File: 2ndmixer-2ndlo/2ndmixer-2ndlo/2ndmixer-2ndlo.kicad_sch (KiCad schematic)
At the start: 44 parts, among them J201 Coax Solder Point, J202 Conn_01x02, J203 Coax Solder Point, Q201 2N5179, Q202 2N5109, T201 Bifilar_Transformer, U201 MAV-11BSM+, U202 TUF-1H+, Y201 100MHz

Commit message: minor fixes to 2ndmixer-2ndlo
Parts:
- C202, C203, C204, C205, C207, C208, C209, C210, C211, C212, C213, C214, C215: footprint (none) -> Capacitor_THT:C_Disc_D5.0mm_W2.5mm_P5.00mm
- C206: footprint (none) -> 2ndmixer-2ndlo:GKG60015
- L201, L202, L203: footprint (none) -> Inductor_THT:L_Toroid_Vertical_L13.0mm_W6.5mm_P5.60mm
- Q201: footprint TO127P584H533-4N -> 2ndmixer-2ndlo:TO127P584H533-4N
- Q202: footprint TO5A -> 2ndmixer-2ndlo:TO5A
- R201, R202, R203, R204, R205, R206, R207, R208, R209, R210, R211, R212, R213, R214, R215, R216, R217: footprint (none) -> Resistor_THT:R_Axial_DIN0207_L6.3mm_D2.5mm_P7.62mm_Horizontal
- T201: footprint (none) -> Transformer_THT:Autotransformer_Toroid_1Tap_Horizontal_D10.5mm_Amidon-T37
- U201: footprint RRR137_MNC -> 2ndmixer-2ndlo:MAV-11BSM&plus_

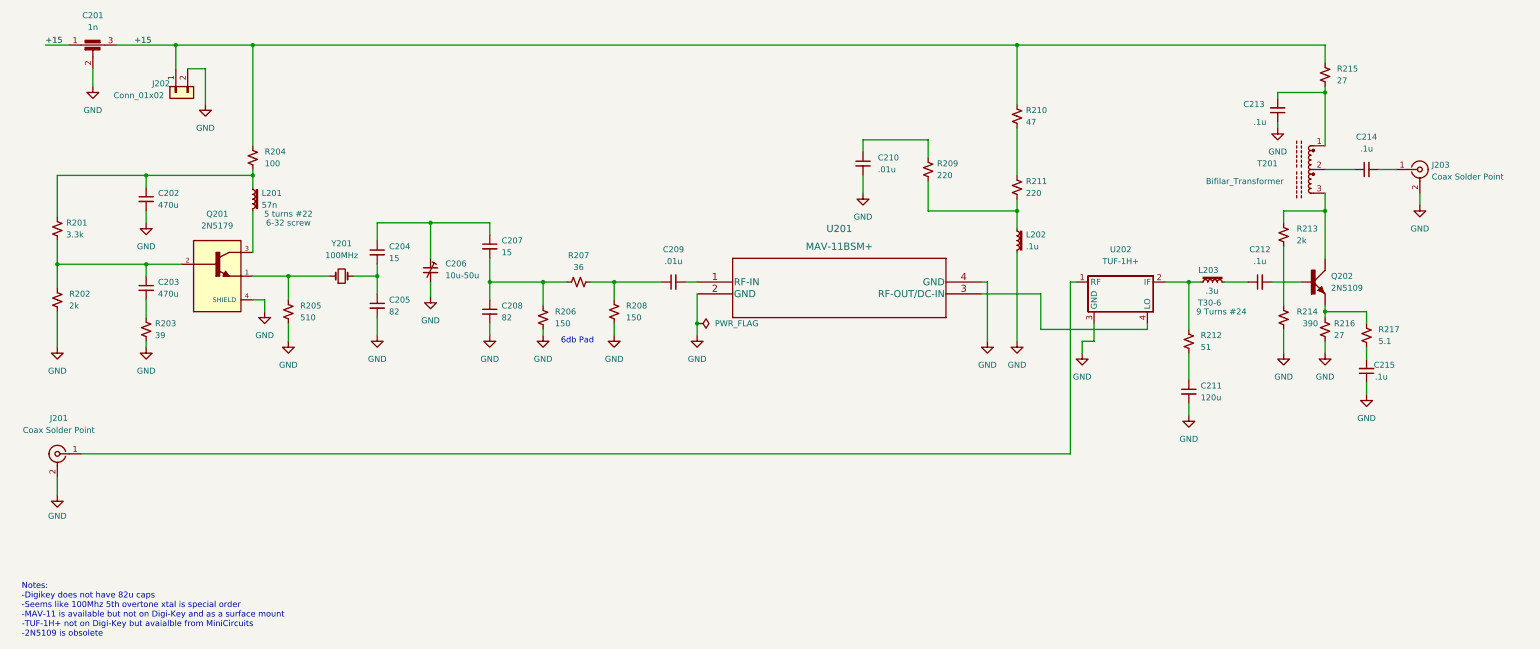
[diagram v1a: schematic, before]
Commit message: made 4 changes to schematic
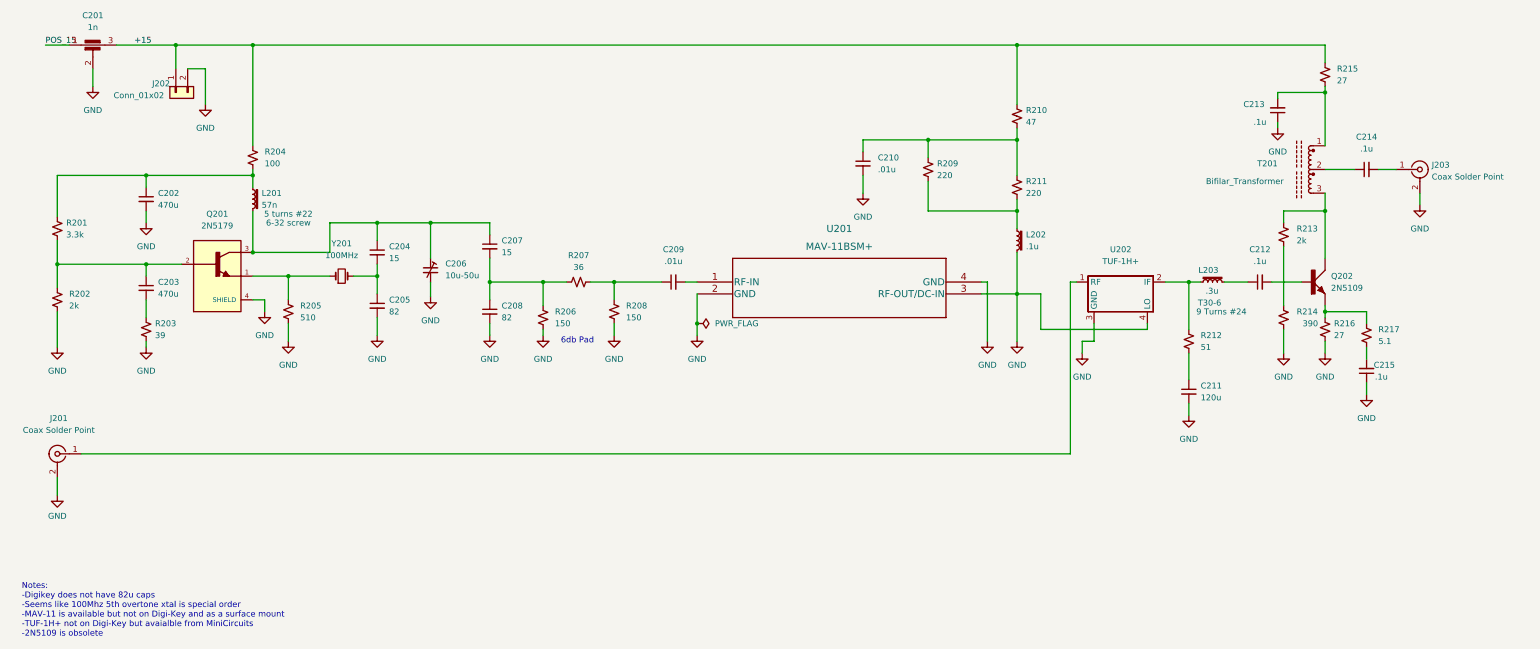
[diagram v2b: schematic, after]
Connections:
- net +15: no longer C201.1
- net GND: now also U201.3 (RF-OUT/DC-IN), U202.4 (LO)
- net at C210.1, R209.1: now also R210.2, R211.1
- net at C204.1, C206.1, C207.1: now also L201.2, Q201.3
- new net POS_15: C201.1
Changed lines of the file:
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@@
   (junction (at 161.29 129.54) (diameter 0) (color 0 0 0 0)
   )
+  (junction (at 66.04 114.3) (diameter 0) (color 0 0 0 0)
+  )
+  (junction (at 229.87 90.17) (diameter 0) (color 0 0 0 0)
+  )
+  (junction (at 92.71 107.95) (diameter 0) (color 0 0 0 0)
+  )
   (junction (at 73.66 119.38) (diameter 0) (color 0 0 0 0)
   )
@@
   (junction (at 229.87 105.41) (diameter 0) (color 0 0 0 0)
   )
+  (junction (at 210.82 90.17) (diameter 0) (color 0 0 0 0)
+  )
+  (junction (at 229.87 123.19) (diameter 0) (color 0 0 0 0)
+  )
   (wire (pts (xy 143.51 120.65) (xy 138.43 120.65))
     (stroke (width 0) (type default) (color 0 0 0 0))
@@
     (stroke (width 0) (type default) (color 0 0 0 0))
   )
-  (wire (pts (xy 222.25 123.19) (xy 234.95 123.19))
+  (wire (pts (xy 222.25 123.19) (xy 229.87 123.19))
     (stroke (width 0) (type default) (color 0 0 0 0))
   )
@@
     (stroke (width 0) (type default) (color 0 0 0 0))
   )
+  (wire (pts (xy 229.87 90.17) (xy 229.87 87.63))
+    (stroke (width 0) (type default) (color 0 0 0 0))
+  )
   (wire (pts (xy 116.84 115.57) (xy 116.84 120.65))
     (stroke (width 0) (type default) (color 0 0 0 0))
@@
     (stroke (width 0) (type default) (color 0 0 0 0))
   )
+  (wire (pts (xy 82.55 114.3) (xy 82.55 107.95))
+    (stroke (width 0) (type default) (color 0 0 0 0))
+  )
   (wire (pts (xy 24.13 162.56) (xy 24.13 166.37))
     (stroke (width 0) (type default) (color 0 0 0 0))
   )
+  (wire (pts (xy 82.55 107.95) (xy 92.71 107.95))
+    (stroke (width 0) (type default) (color 0 0 0 0))
+  )
   (wire (pts (xy 55.88 74.93) (xy 55.88 82.55))
     (stroke (width 0) (type default) (color 0 0 0 0))
   )
+  (wire (pts (xy 66.04 114.3) (xy 82.55 114.3))
+    (stroke (width 0) (type default) (color 0 0 0 0))
+  )
   (wire (pts (xy 222.25 120.65) (xy 223.52 120.65))
     (stroke (width 0) (type default) (color 0 0 0 0))
@@
     (stroke (width 0) (type default) (color 0 0 0 0))
   )
+  (wire (pts (xy 210.82 90.17) (xy 229.87 90.17))
+    (stroke (width 0) (type default) (color 0 0 0 0))
+  )
   (wire (pts (xy 104.14 107.95) (xy 116.84 107.95))
     (stroke (width 0) (type default) (color 0 0 0 0))
@@
     (stroke (width 0) (type default) (color 0 0 0 0))
   )
-  (wire (pts (xy 229.87 114.3) (xy 229.87 133.35))
+  (wire (pts (xy 229.87 114.3) (xy 229.87 123.19))
+    (stroke (width 0) (type default) (color 0 0 0 0))
+  )
+  (wire (pts (xy 229.87 123.19) (xy 229.87 133.35))
     (stroke (width 0) (type default) (color 0 0 0 0))
   )
@@
     (stroke (width 0) (type default) (color 0 0 0 0))
   )
-  (wire (pts (xy 229.87 97.79) (xy 229.87 87.63))
+  (wire (pts (xy 229.87 97.79) (xy 229.87 90.17))
     (stroke (width 0) (type default) (color 0 0 0 0))
   )
@@
   )
   (wire (pts (xy 43.18 134.62) (xy 43.18 133.35))
+    (stroke (width 0) (type default) (color 0 0 0 0))
+  )
+  (wire (pts (xy 229.87 123.19) (xy 234.95 123.19))
     (stroke (width 0) (type default) (color 0 0 0 0))
   )
@@
     (effects (font (size 1.27 1.27)) (justify left bottom))
   )
-  (label "+15" (at 21.59 69.85 0)
+  (label "POS_15" (at 21.59 69.85 0)
     (effects (font (size 1.27 1.27)) (justify left bottom))
   )

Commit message: 2ndmixer-2ndlo layout
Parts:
- added H201, H202, H203, H204: MountingHole, MountingHole:MountingHole_3.2mm_M3, symbol Mechanical:MountingHole
- U202: footprint (none) -> 2ndmixer-2ndlo:TUF-1H
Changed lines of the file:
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@@
+    (stroke (width 0) (type default) (color 0 0 0 0))
+  )
+  (polyline (pts (xy 139.7 181.61) (xy 139.7 194.31))
     (stroke (width 0) (type default) (color 0 0 0 0))
   )
@@
     (stroke (width 0) (type default) (color 0 0 0 0))
   )
+  (polyline (pts (xy 172.085 181.61) (xy 215.265 181.61))
+    (stroke (width 0) (type default) (color 0 0 0 0))
+  )
   (wire (pts (xy 82.55 114.3) (xy 82.55 107.95))
     (stroke (width 0) (type default) (color 0 0 0 0))
@@
     (stroke (width 0) (type default) (color 0 0 0 0))
   )
+  (polyline (pts (xy 215.265 181.61) (xy 215.265 194.31))
+    (stroke (width 0) (type default) (color 0 0 0 0))
+  )
   (wire (pts (xy 304.8 127) (xy 295.91 127))
     (stroke (width 0) (type default) (color 0 0 0 0))
@@
     (stroke (width 0) (type default) (color 0 0 0 0))
   )
+  (polyline (pts (xy 215.265 194.31) (xy 139.065 194.31))
+    (stroke (width 0) (type default) (color 0 0 0 0))
+  )
   (wire (pts (xy 210.82 99.06) (xy 210.82 105.41))
     (stroke (width 0) (type default) (color 0 0 0 0))
@@
   )
   (wire (pts (xy 43.18 97.79) (xy 66.04 97.79))
+    (stroke (width 0) (type default) (color 0 0 0 0))
+  )
+  (polyline (pts (xy 172.085 181.61) (xy 139.065 181.61))
     (stroke (width 0) (type default) (color 0 0 0 0))
   )
@@
     (pin "2")
   )
+  (symbol (lib_id "Mechanical:MountingHole") (at 178.435 189.23 0) (unit 1)
+    (in_bom yes) (on_board yes) (fields_autoplaced)
+    (property "Reference" "H203" (id 0) (at 180.975 187.9599 0)
+      (effects (font (size 1.27 1.27)) (justify left))
+    )
+    (property "Value" "MountingHole" (id 1) (at 180.975 190.4999 0)
+      (effects (font (size 1.27 1.27)) (justify left))
+    )
+    (property "Footprint" "MountingHole:MountingHole_3.2mm_M3" (id 2) (at 178.435 189.23 0)
+      (effects (font (size 1.27 1.27)) hide)
+    )
+    (property "Datasheet" "~" (id 3) (at 178.435 189.23 0)
+      (effects (font (size 1.27 1.27)) hide)
+    )
+  )
   (symbol (lib_id "power:GND") (at 43.18 134.62 0) (unit 1)
     (in_bom yes) (on_board yes) (fields_autoplaced)
@@
     (property "Reference" "U202" (id 0) (at 252.095 113.665 0))
     (property "Value" "TUF-1H+" (id 1) (at 252.095 116.205 0))
-    (property "Footprint" "" (id 2) (at 251.46 123.19 0)
+    (property "Footprint" "2ndmixer-2ndlo:TUF-1H" (id 2) (at 251.46 123.19 0)
       (effects (font (size 1.27 1.27)) hide)
     )
@@
     (pin "2")
   )
+  (symbol (lib_id "Mechanical:MountingHole") (at 142.875 189.23 0) (unit 1)
+    (in_bom yes) (on_board yes) (fields_autoplaced)
+    (property "Reference" "H201" (id 0) (at 145.415 187.9599 0)
+      (effects (font (size 1.27 1.27)) (justify left))
+    )
+    (property "Value" "MountingHole" (id 1) (at 145.415 190.4999 0)
+      (effects (font (size 1.27 1.27)) (justify left))
+    )
+    (property "Footprint" "MountingHole:MountingHole_3.2mm_M3" (id 2) (at 142.875 189.23 0)
+      (effects (font (size 1.27 1.27)) hide)
+    )
+    (property "Datasheet" "~" (id 3) (at 142.875 189.23 0)
+      (effects (font (size 1.27 1.27)) hide)
+    )
+  )
   (symbol (lib_id "Device:R_Small_US") (at 66.04 93.98 0) (unit 1)
     (in_bom yes) (on_board yes) (fields_autoplaced)
@@
     (pin "2")
   )
+  (symbol (lib_id "Mechanical:MountingHole") (at 160.655 189.23 0) (unit 1)
+    (in_bom yes) (on_board yes) (fields_autoplaced)
+    (property "Reference" "H202" (id 0) (at 163.195 187.9599 0)
+      (effects (font (size 1.27 1.27)) (justify left))
+    )
+    (property "Value" "MountingHole" (id 1) (at 163.195 190.4999 0)
+      (effects (font (size 1.27 1.27)) (justify left))
+    )
+    (property "Footprint" "MountingHole:MountingHole_3.2mm_M3" (id 2) (at 160.655 189.23 0)
+      (effects (font (size 1.27 1.27)) hide)
+    )
+    (property "Datasheet" "~" (id 3) (at 160.655 189.23 0)
+      (effects (font (size 1.27 1.27)) hide)
+    )
+  )
   (symbol (lib_id "Device:C_Small") (at 43.18 102.87 0) (unit 1)
     (in_bom yes) (on_board yes) (fields_autoplaced)
@@
     )
     (pin "1")
+  )
+  (symbol (lib_id "Mechanical:MountingHole") (at 197.485 189.23 0) (unit 1)
+    (in_bom yes) (on_board yes) (fields_autoplaced)
+    (property "Reference" "H204" (id 0) (at 200.025 187.9599 0)
+      (effects (font (size 1.27 1.27)) (justify left))
+    )
+    (property "Value" "MountingHole" (id 1) (at 200.025 190.4999 0)
+      (effects (font (size 1.27 1.27)) (justify left))
+    )
+    (property "Footprint" "MountingHole:MountingHole_3.2mm_M3" (id 2) (at 197.485 189.23 0)
+      (effects (font (size 1.27 1.27)) hide)
+    )
+    (property "Datasheet" "~" (id 3) (at 197.485 189.23 0)
+      (effects (font (size 1.27 1.27)) hide)
+    )
   )
   (symbol (lib_id "2022-08-04_19-42-18:MAV-11BSM+") (at 161.29 120.65 0) (unit 1)
@@
       (reference "C215") (unit 1) (value ".1u") (footprint "Capacitor_THT:C_Disc_D5.0mm_W2.5mm_P5.00mm")
     )
+    (path "/c00c0b05-feed-40a4-a5ca-549d29aee4ea"
+      (reference "H201") (unit 1) (value "MountingHole") (footprint "MountingHole:MountingHole_3.2mm_M3")
+    )
+    (path "/daf66e9c-431d-41d1-8614-1969dbafecf1"
+      (reference "H202") (unit 1) (value "MountingHole") (footprint "MountingHole:MountingHole_3.2mm_M3")
+    )
+    (path "/3b81682e-613a-49c1-b994-5598a0e69dc7"
+      (reference "H203") (unit 1) (value "MountingHole") (footprint "MountingHole:MountingHole_3.2mm_M3")
+    )
+    (path "/eb89cc5b-a0e6-4666-80e2-bbd85deb6860"
+      (reference "H204") (unit 1) (value "MountingHole") (footprint "MountingHole:MountingHole_3.2mm_M3")
+    )
     (path "/d9383354-86b1-4e1b-8d1a-635f4cf9a02f"
       (reference "J201") (unit 1) (value "Coax Solder Point") (footprint "Connector_Wire:SolderWire-0.5sqmm_1x02_P4.6mm_D0.9mm_OD2.1mm")
@@
     )
     (path "/4b92b6cd-ecaa-4fa9-91f6-6c221e287382"
-      (reference "U202") (unit 1) (value "TUF-1H+") (footprint "")
+      (reference "U202") (unit 1) (value "TUF-1H+") (footprint "2ndmixer-2ndlo:TUF-1H")
     )
     (path "/403086ff-cfdb-4174-9122-d835880b0ac5"

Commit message: various updates
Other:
- title: Spectrum Analyzer: Second Mixer and Second Local Analyzer -> Spectrum Analyzer: Second Mixer and Second Local Oscillator
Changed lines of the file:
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@@
   (paper "USLegal")
   (title_block
-    (title "Spectrum Analyzer: Second Mixer and Second Local Analyzer")
+    (title "Spectrum Analyzer: Second Mixer and Second Local Oscillator")
     (date "2022-08-04")
     (rev "0")

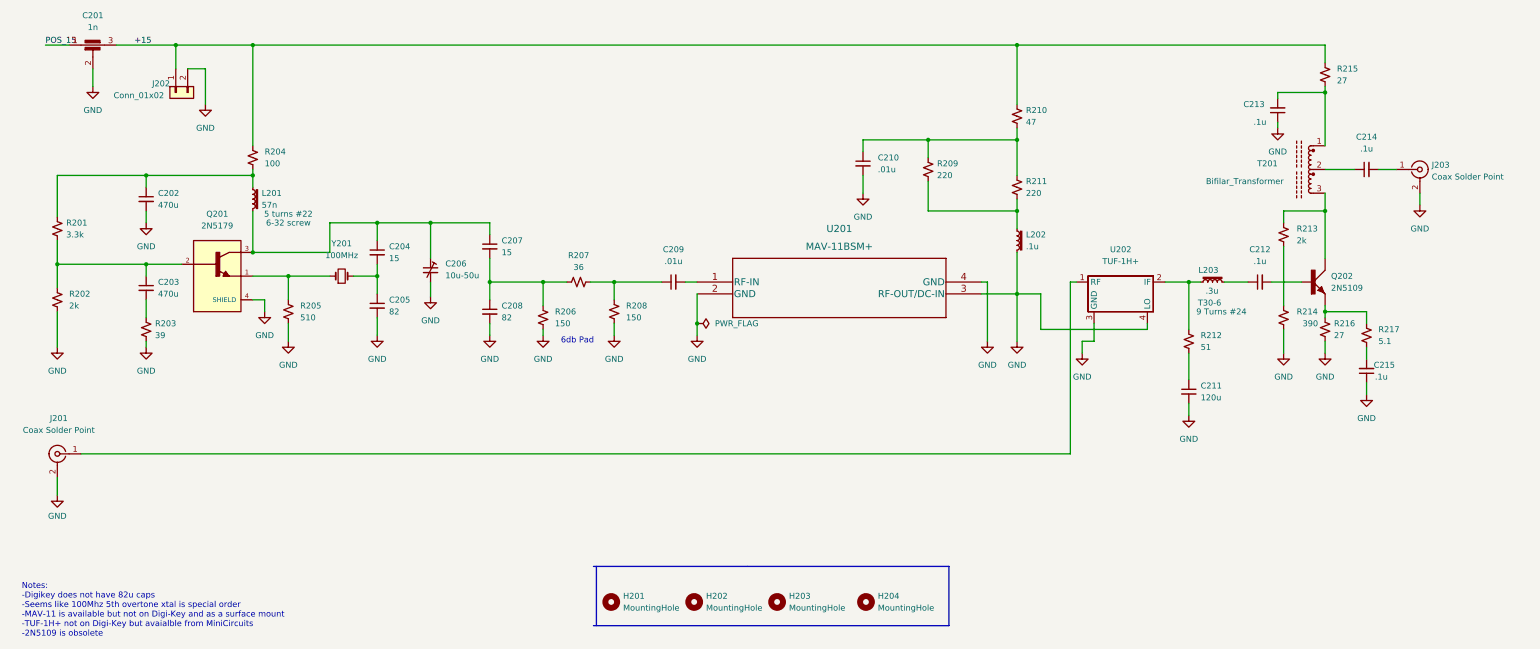
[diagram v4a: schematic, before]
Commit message: improved if and log amp and second lo/mixer
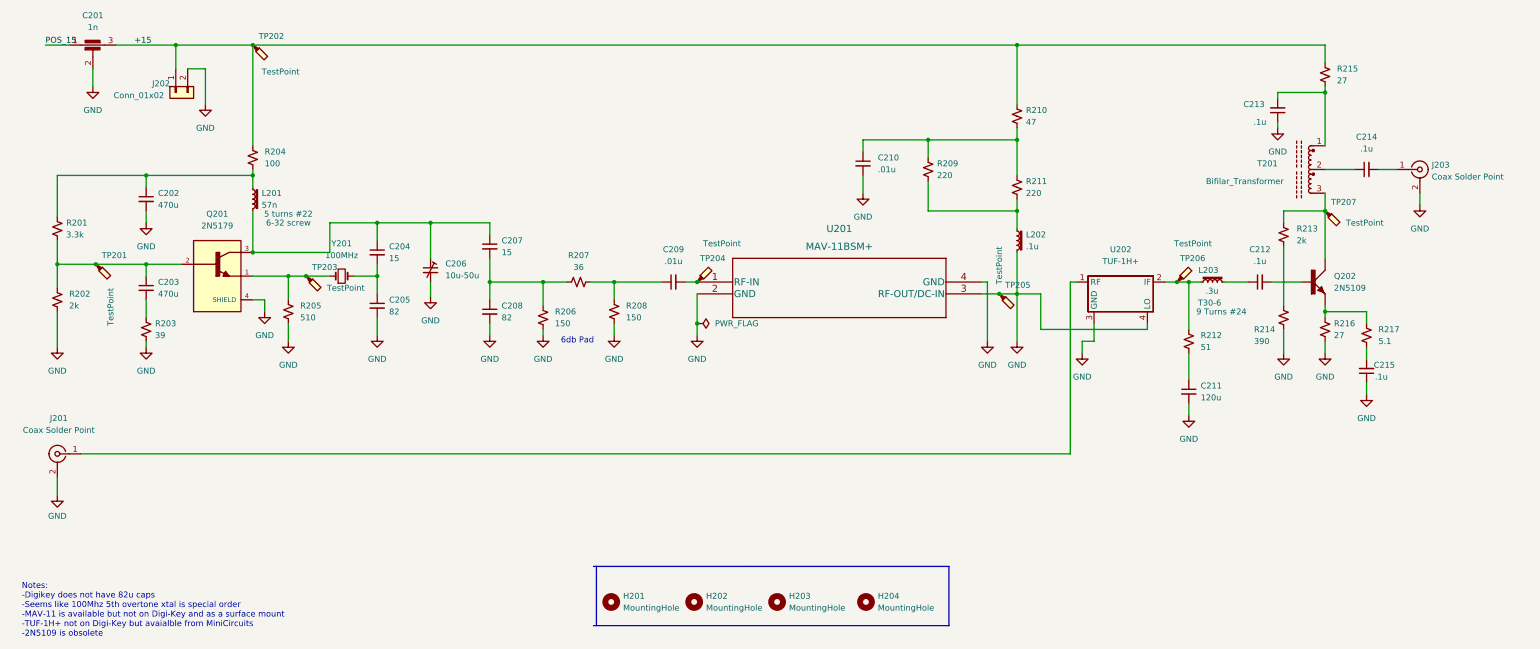
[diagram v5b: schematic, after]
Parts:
- added TP201, TP202, TP203, TP204, TP205, TP206, TP207: TestPoint, TestPoint:TestPoint_Pad_1.0x1.0mm, symbol Connector:TestPoint_Probe
- Q202: footprint 2ndmixer-2ndlo:TO5A -> TO5A
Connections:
- net +15: now also TP202.1
- net GND: now also TP205.1
- net at C209.2, U201.1 (RF-IN): now also TP204.1
- net at Q202.C, R213.1, T201.3: now also TP207.1
- net at L203.1, R212.1, U202.2 (IF): now also TP206.1
- net at Q201.1, R205.1, Y201.1: now also TP203.1
- net at C203.1, Q201.2, R201.2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: now also TP201.1
